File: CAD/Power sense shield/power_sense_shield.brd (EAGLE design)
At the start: 41.5 x 35.4 mm, 2 parts

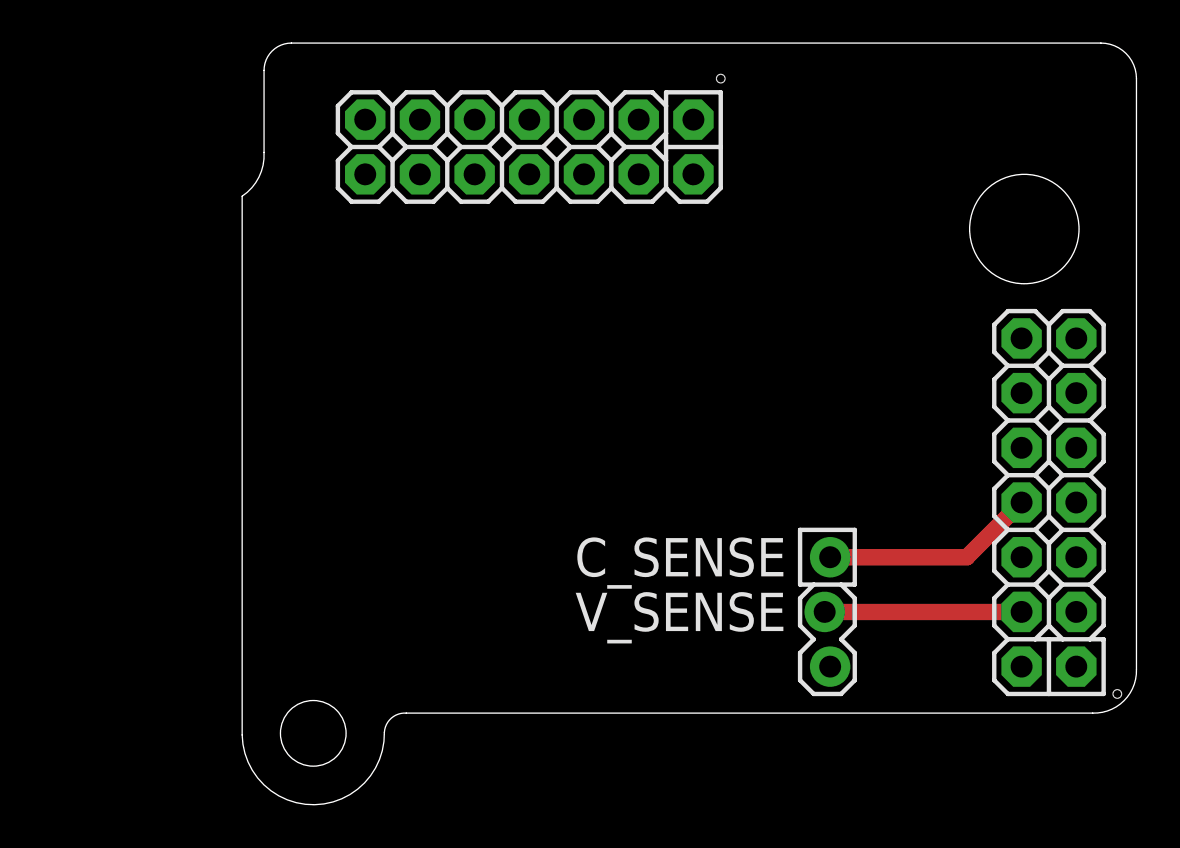
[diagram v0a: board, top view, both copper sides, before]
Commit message: Updated the power sense board to the v3 CANode shield layout.
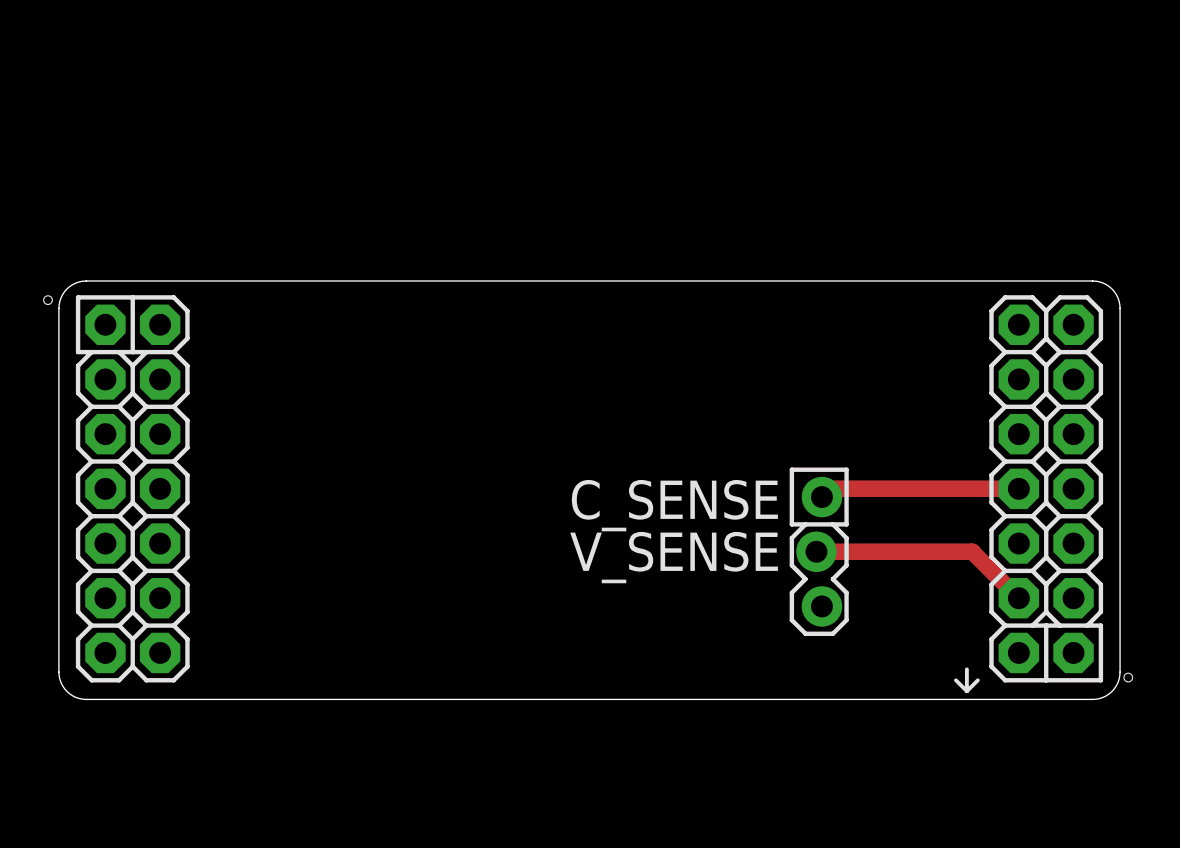
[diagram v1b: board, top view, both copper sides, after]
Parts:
- JP1: value (none) -> M03LOCK
- U$1: value CAN_NODE_SHIELD -> CANODE_SHIELD; device ASL:CAN_NODE_SHIELD -> ASL:CANODE_SHIELD
- moved JP1 2.82 mm to (35.6, 16.1)
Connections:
- net N$2: now also U$1.A0; no longer U$1.P$4
- net N$3: now also U$1.RB1; no longer U$1.P$8
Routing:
- net N$2: track 9.14 -> 10.3 mm
- net N$3: track 9.94 -> 9.30 mm
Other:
- board size 41.5 x 35.4 mm -> 49.3 x 19.4 mm
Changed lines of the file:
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@@
 <setting verticaltext="up"/>
 </settings>
-<grid distance="0.005" unitdist="inch" unit="inch" style="lines" multiple="1" display="no" altdistance="0.025" altunitdist="inch" altunit="inch"/>
+<grid distance="0.01" unitdist="inch" unit="inch" style="lines" multiple="1" display="no" altdistance="0.025" altunitdist="inch" altunit="inch"/>
 <layers>
 <layer number="1" name="Top" color="4" fill="1" visible="yes" active="yes"/>
@@
 <board>
 <plain>
-<text x="34.036" y="11.684" size="1.778" layer="21" font="vector" ratio="12" rot="R180">V_SENSE</text>
-<text x="34.036" y="14.224" size="1.778" layer="21" font="vector" ratio="12" rot="R180">C_SENSE</text>
+<text x="33.782" y="14.478" size="1.778" layer="21" font="vector" ratio="12" rot="R180">V_SENSE</text>
+<text x="33.782" y="16.891" size="1.778" layer="21" font="vector" ratio="12" rot="R180">C_SENSE</text>
+<wire x1="0.254" y1="24.892" x2="0.254" y2="8.001" width="0" layer="20"/>
+<wire x1="0.254" y1="8.001" x2="1.524" y2="6.731" width="0" layer="20" curve="90"/>
+<wire x1="1.524" y1="6.731" x2="48.26" y2="6.731" width="0" layer="20"/>
+<wire x1="48.26" y1="6.731" x2="49.53" y2="8.001" width="0" layer="20" curve="90"/>
+<wire x1="49.53" y1="8.001" x2="49.53" y2="24.892" width="0" layer="20"/>
+<wire x1="49.53" y1="24.892" x2="48.26" y2="26.162" width="0" layer="20" curve="90"/>
+<wire x1="48.26" y1="26.162" x2="1.524" y2="26.162" width="0" layer="20"/>
+<wire x1="1.524" y1="26.162" x2="0.254" y2="24.892" width="0" layer="20" curve="90"/>
+<wire x1="42.418" y1="7.112" x2="42.418" y2="8.128" width="0.1778" layer="21"/>
+<wire x1="42.418" y1="7.112" x2="42.926" y2="7.62" width="0.1778" layer="21"/>
+<wire x1="42.418" y1="7.112" x2="41.91" y2="7.62" width="0.1778" layer="21"/>
 </plain>
 <attributes>
@@
 </autorouter>
 <elements>
-<element name="U$1" library="ASL" package="CAN_NODE_SHIELD" value="CAN_NODE_SHIELD" x="0" y="0"/>
-<element name="JP1" library="ASL" package="1X03_LOCK" value="" x="35.941" y="13.335" smashed="yes" rot="R270"/>
+<element name="U$1" library="ASL" package="CANODE_SHIELD" value="CANODE_SHIELD" x="0" y="0"/>
+<element name="JP1" library="ASL" package="1X03_LOCK" value="M03LOCK" x="35.56" y="16.129" smashed="yes" rot="R270"/>
 </elements>
 <signals>
 <signal name="N$3" class="2">
-<contactref element="U$1" pad="P$8"/>
+<contactref element="U$1" pad="RB1"/>
 <contactref element="JP1" pad="1"/>
-<wire x1="36.068" y1="13.335" x2="42.418" y2="13.335" width="0.762" layer="1"/>
-<wire x1="42.418" y1="13.335" x2="44.958" y2="15.875" width="0.762" layer="1"/>
+<wire x1="35.687" y1="16.129" x2="36.068" y2="16.51" width="0.762" layer="1"/>
+<wire x1="36.068" y1="16.51" x2="44.831" y2="16.51" width="0.762" layer="1"/>
 </signal>
 <signal name="N$2">
-<contactref element="U$1" pad="P$4"/>
+<contactref element="U$1" pad="A0"/>
 <contactref element="JP1" pad="2"/>
-<wire x1="35.814" y1="10.795" x2="44.958" y2="10.795" width="0.762" layer="1"/>
+<wire x1="44.831" y1="11.43" x2="42.672" y2="13.589" width="0.762" layer="1"/>
+<wire x1="42.672" y1="13.589" x2="35.433" y2="13.589" width="0.762" layer="1"/>
 </signal>
 </signals>

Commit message: Updated all CANode shields to fit the latest version of it.
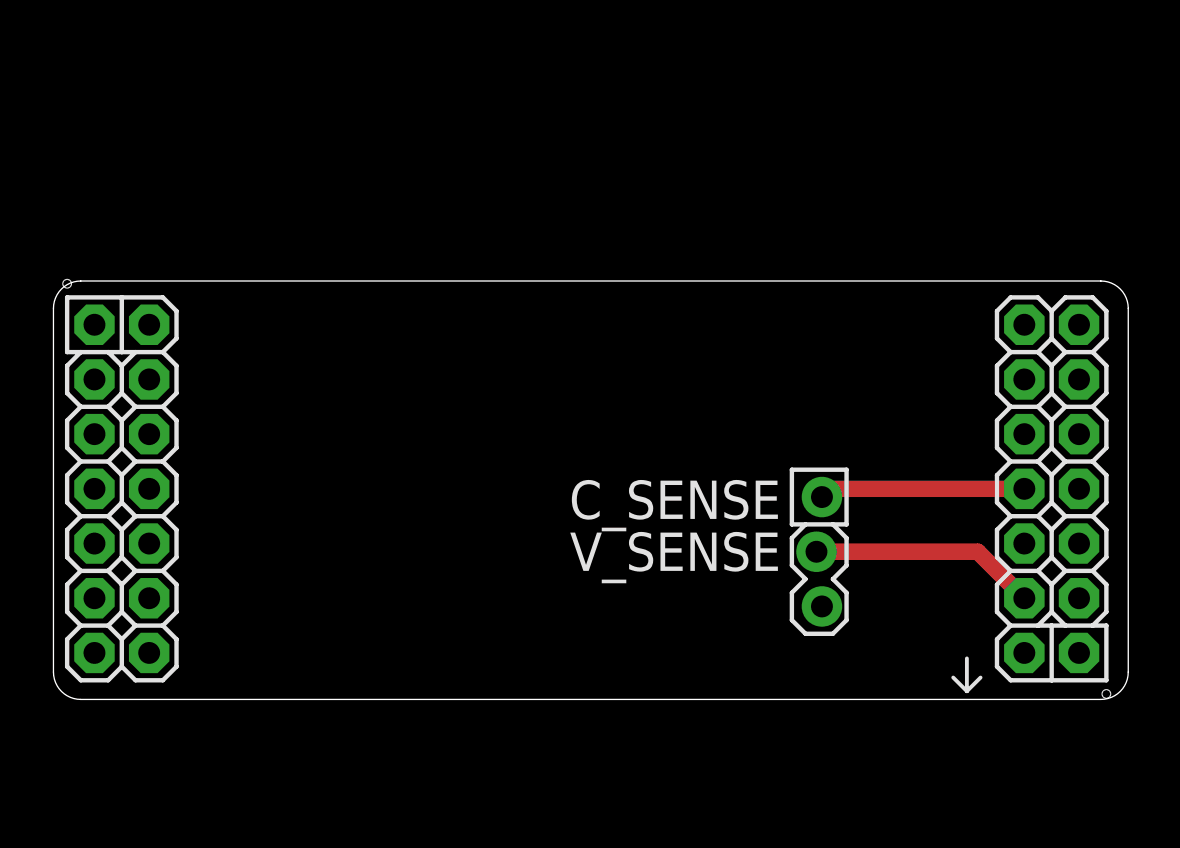
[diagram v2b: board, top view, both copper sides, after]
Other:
- board size 49.3 x 19.4 mm -> 49.9 x 19.4 mm
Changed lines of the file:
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@@
 <setting verticaltext="up"/>
 </settings>
-<grid distance="0.01" unitdist="inch" unit="inch" style="lines" multiple="1" display="no" altdistance="0.025" altunitdist="inch" altunit="inch"/>
+<grid distance="0.005" unitdist="inch" unit="inch" style="lines" multiple="1" display="no" altdistance="0.025" altunitdist="inch" altunit="inch"/>
 <layers>
 <layer number="1" name="Top" color="4" fill="1" visible="yes" active="yes"/>
@@
 <text x="33.782" y="14.478" size="1.778" layer="21" font="vector" ratio="12" rot="R180">V_SENSE</text>
 <text x="33.782" y="16.891" size="1.778" layer="21" font="vector" ratio="12" rot="R180">C_SENSE</text>
-<wire x1="0.254" y1="24.892" x2="0.254" y2="8.001" width="0" layer="20"/>
-<wire x1="0.254" y1="8.001" x2="1.524" y2="6.731" width="0" layer="20" curve="90"/>
-<wire x1="1.524" y1="6.731" x2="48.26" y2="6.731" width="0" layer="20"/>
-<wire x1="48.26" y1="6.731" x2="49.53" y2="8.001" width="0" layer="20" curve="90"/>
-<wire x1="49.53" y1="8.001" x2="49.53" y2="24.892" width="0" layer="20"/>
-<wire x1="49.53" y1="24.892" x2="48.26" y2="26.162" width="0" layer="20" curve="90"/>
-<wire x1="48.26" y1="26.162" x2="1.524" y2="26.162" width="0" layer="20"/>
-<wire x1="1.524" y1="26.162" x2="0.254" y2="24.892" width="0" layer="20" curve="90"/>
-<wire x1="42.418" y1="7.112" x2="42.418" y2="8.128" width="0.1778" layer="21"/>
-<wire x1="42.418" y1="7.112" x2="42.926" y2="7.62" width="0.1778" layer="21"/>
-<wire x1="42.418" y1="7.112" x2="41.91" y2="7.62" width="0.1778" layer="21"/>
+<wire x1="0" y1="24.892" x2="0" y2="8.001" width="0" layer="20"/>
+<wire x1="0" y1="8.001" x2="1.27" y2="6.731" width="0" layer="20" curve="90"/>
+<wire x1="1.27" y1="6.731" x2="48.641" y2="6.731" width="0" layer="20"/>
+<wire x1="48.641" y1="6.731" x2="49.911" y2="8.001" width="0" layer="20" curve="90"/>
+<wire x1="49.911" y1="8.001" x2="49.911" y2="24.892" width="0" layer="20"/>
+<wire x1="49.911" y1="24.892" x2="48.641" y2="26.162" width="0" layer="20" curve="90"/>
+<wire x1="48.641" y1="26.162" x2="1.27" y2="26.162" width="0" layer="20"/>
+<wire x1="1.27" y1="26.162" x2="0" y2="24.892" width="0" layer="20" curve="90"/>
+<wire x1="42.418" y1="7.112" x2="42.418" y2="8.636" width="0.1778" layer="21"/>
+<wire x1="42.418" y1="7.112" x2="43.053" y2="7.747" width="0.1778" layer="21"/>
+<wire x1="42.418" y1="7.112" x2="41.783" y2="7.747" width="0.1778" layer="21"/>
 </plain>
 <attributes>
@@
 <contactref element="JP1" pad="1"/>
 <wire x1="35.687" y1="16.129" x2="36.068" y2="16.51" width="0.762" layer="1"/>
-<wire x1="36.068" y1="16.51" x2="44.831" y2="16.51" width="0.762" layer="1"/>
+<wire x1="36.068" y1="16.51" x2="45.085" y2="16.51" width="0.762" layer="1"/>
 </signal>
 <signal name="N$2">
 <contactref element="U$1" pad="A0"/>
 <contactref element="JP1" pad="2"/>
-<wire x1="44.831" y1="11.43" x2="42.672" y2="13.589" width="0.762" layer="1"/>
-<wire x1="42.672" y1="13.589" x2="35.433" y2="13.589" width="0.762" layer="1"/>
+<wire x1="45.085" y1="11.43" x2="42.926" y2="13.589" width="0.762" layer="1"/>
+<wire x1="42.926" y1="13.589" x2="35.433" y2="13.589" width="0.762" layer="1"/>
 </signal>
 </signals>
